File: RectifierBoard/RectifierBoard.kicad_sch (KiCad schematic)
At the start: 14 parts, among them J1 MKDS 1,5/2-7,62, J2 MKDS 5/ 4-7,62, J3 B+PI, J4 B+ Preamp

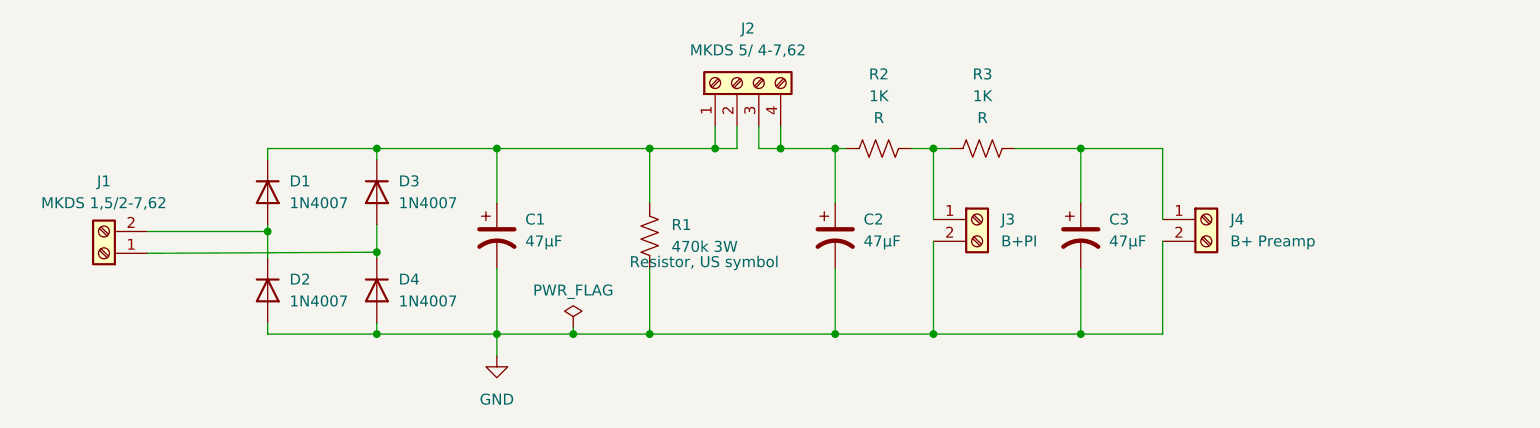
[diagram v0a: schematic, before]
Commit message: First cut at PCB layout
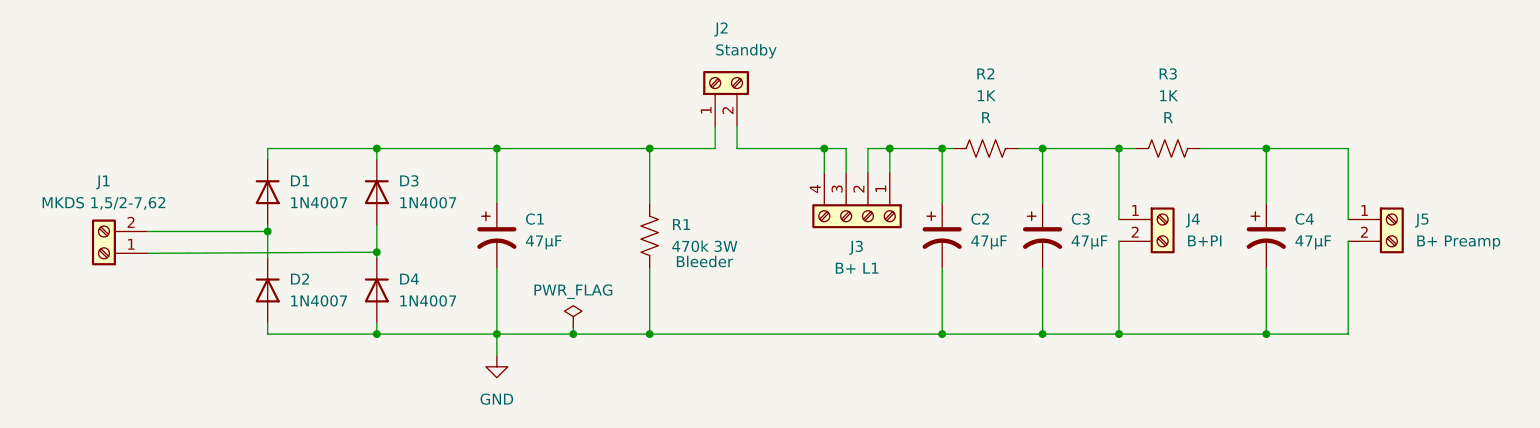
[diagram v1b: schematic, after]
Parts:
- added C3: 47µF, Capacitor_THT:CP_Radial_D18.0mm_P7.50mm, symbol Device:C_Polarized_US
- added J2: Standby, TerminalBlock_508:MKDS 5_2-7,62, symbol Connector:Screw_Terminal_01x02
- J3: renamed from J2; value MKDS 5/ 4-7,62 -> B+ L1
- renumbered C3 to C4, J3 to J4, J4 to J5
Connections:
- net GND: now also C3.2
- net at C1.1, D1.1 (K), D3.1 (K)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: now also J2.1 (Pin_1); no longer J3.1 (Pin_1), J3.2 (Pin_2)
- net at J3.3 (Pin_3), J3.4 (Pin_4): now also J2.2 (Pin_2); no longer C2.1, R2.1
- net at J4.1 (Pin_1), R2.2, R3.1: now also C3.1
- new net: C2.1, J3.1 (Pin_1), J3.2 (Pin_2), R2.1
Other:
- moved on the sheet: C2, C4, J3, J4, J5, R2, R3

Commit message: Layout  - CORRECT GROUND ISSUE NEXT !!!!
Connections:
- net B+_PREAMP: now reaches C4.1, J5.1 (Pin_1), R3.2
- net B+_PRE_STBY: now reaches C1.1, D1.1 (K), D3.1 (K), R1.1
- net B+_PRE_STBY: now also J2.2 (Pin_2); no longer J2.1 (Pin_1)
- net HT_AC_B: now reaches D1.2 (A), D2.1 (K), J1.2 (Pin_2)
- net HT_AC_A: now reaches D3.2 (A), D4.1 (K), J1.1 (Pin_1)
- net B+_STBY_OUT: now reaches J3.3 (Pin_3), J3.4 (Pin_4)
- net B+_STBY_OUT: now also J2.1 (Pin_1); no longer J2.2 (Pin_2)
- net B+_PI: now reaches C3.1, J4.1 (Pin_1), R2.2, R3.1
- net B+_L1_OUT: now reaches C2.1, J3.1 (Pin_1), J3.2 (Pin_2), R2.1
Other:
- moved on the sheet: J2
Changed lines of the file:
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@@
-	(wire
-		(pts
-			(xy 154.94 63.5) (xy 154.94 60.96)
-		)
-		(stroke
-			(width 0)
-			(type default)
-		)
-	)
 	(wire
 		(pts
@@
 	(wire
 		(pts
-			(xy 152.4 63.5) (xy 152.4 60.96)
-		)
-		(stroke
-			(width 0)
-			(type default)
-		)
-	)
-	(wire
-		(pts
 			(xy 199.39 63.5) (xy 201.295 63.5)
 		)
@@
 	(wire
 		(pts
+			(xy 154.94 63.5) (xy 154.94 66.294)
+		)
+		(stroke
+			(width 0)
+			(type default)
+		)
+	)
+	(wire
+		(pts
 			(xy 199.39 85.09) (xy 216.535 85.09)
 		)
@@
 	(wire
 		(pts
+			(xy 152.4 66.294) (xy 152.4 63.5)
+		)
+		(stroke
+			(width 0)
+			(type default)
+		)
+	)
+	(wire
+		(pts
 			(xy 127 85.09) (xy 135.89 85.09)
 		)
@@
 			(width 0)
 			(type default)
+		)
+	)
+	(label "B+_PI"
+		(at 199.39 69.088 0)
+		(effects
+			(font
+				(size 1.27 1.27)
+			)
+			(justify left bottom)
+		)
+	)
+	(label "B+_STBY_OUT"
+		(at 154.94 63.5 0)
+		(effects
+			(font
+				(size 1.27 1.27)
+			)
+			(justify left bottom)
+		)
+	)
+	(label "B+_PRE_STBY"
+		(at 117.348 63.5 0)
+		(effects
+			(font
+				(size 1.27 1.27)
+			)
+			(justify left bottom)
+		)
+	)
+	(label "HT_AC_A"
+		(at 113.03 74.422 0)
+		(effects
+			(font
+				(size 1.27 1.27)
+			)
+			(justify left bottom)
+		)
+	)
+	(label "B+_PREAMP"
+		(at 226.06 68.58 0)
+		(effects
+			(font
+				(size 1.27 1.27)
+			)
+			(justify left bottom)
+		)
+	)
+	(label "HT_AC_B"
+		(at 87.122 73.152 0)
+		(effects
+			(font
+				(size 1.27 1.27)
+			)
+			(justify left bottom)
+		)
+	)
+	(label "B+_L1_OUT"
+		(at 170.18 63.5 0)
+		(effects
+			(font
+				(size 1.27 1.27)
+			)
+			(justify left bottom)
 		)
 	)
@@
 	(symbol
 		(lib_id "Connector:Screw_Terminal_01x02")
-		(at 152.4 55.88 90)
+		(at 154.94 71.374 270)
 		(unit 1)
 		(body_style 1)
@@
 		(dnp no)
 		(property "Reference" "J2"
-			(at 152.4 49.53 90)
+			(at 155.194 75.184 90)
 			(show_name no)
 			(do_not_autoplace no)
@@
 		)
 		(property "Value" "Standby"
-			(at 152.4 52.07 90)
+			(at 157.988 77.216 90)
 			(show_name no)
 			(do_not_autoplace no)
@@
 		)
 		(property "Footprint" "TerminalBlock_508:MKDS 5_2-7,62"
-			(at 152.4 55.88 0)
+			(at 154.94 71.374 0)
 			(hide yes)
 			(show_name no)
@@
 		)
 		(property "Datasheet" ""
-			(at 152.4 55.88 0)
+			(at 154.94 71.374 0)
 			(hide yes)
 			(show_name no)
@@
 		)
 		(property "Description" "Generic screw terminal, single row, 01x02, script generated (kicad-library-utils/schlib/autogen/connector/)"
-			(at 152.4 55.88 0)
+			(at 154.94 71.374 0)
 			(hide yes)
 			(show_name no)
@@
 		(dnp no)
 		(property "Reference" "R1"
-			(at 147.32 72.3899 0)
+			(at 140.208 71.374 0)
 			(show_name no)
 			(do_not_autoplace no)
@@
 		)
 		(property "Value" "470k 3W"
-			(at 147.32 74.9299 0)
+			(at 147.066 77.724 90)
 			(show_name no)
 			(do_not_autoplace no)
@@
 		)
 		(property "Description" "Bleeder"
-			(at 151.13 76.708 0)
-			(show_name no)
-			(do_not_autoplace no)
+			(at 148.844 73.66 90)
+			(show_name no)
+			(do_not_autoplace no)

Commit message: Getting closer
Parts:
- J5: value B+ Preamp -> GND
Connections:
- net B+_PI: now also J4.2 (Pin_2); no longer J4.1 (Pin_1)
- net B+_PREAMP: now also J4.1 (Pin_1); no longer J5.1 (Pin_1)
- net GND: now also J5.1 (Pin_1); no longer J4.2 (Pin_2)
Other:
- moved on the sheet: C4, J5
